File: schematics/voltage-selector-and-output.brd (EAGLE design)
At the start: 100 x 80 mm, 22 parts, among them IC1 3.3V, IC2 MIC2941, IC4 ULN2003AN, IC6 ATTINY85, IC7 74LS595N

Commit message: Finally updated the primary schematic
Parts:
- removed INPUT: (no value), SparkFun:1X02
- removed ISP1: AVRISP-6, adafruit:AVRISP
- removed JP1: (no value), SparkFun:JST-2-PTH
- removed R11: 10k, rcl-ez:0207/5V
- removed R7: 11k, rcl-ez:0207/5V
- removed R8: 20.5k, rcl-ez:0207/5V
- removed R9: 41.2k, rcl-ez:0207/5V
- removed R97: 6.49K 1%, rcl-ez:0207/5V
- added C1, C4: 47uF/25V, minimidi:E2,5-6
- added C5: 0.1uF, SparkFun-Capacitors:CAP-PTH-SMALL
- added D1, D2, D3, D4: 1N4007, gm-diodes:DO41-3
- added D6: (no value), SparkFun-LED:LED3MM-NS
- added IC3: MCP41010P, microchip-custom:DIL8
- added IC5: 12V, v-reg:78XXS
- added ISP: AVRISP-6, adafruit:AVRISP
- added JACK, XFRM: (no value), SparkFun:1X02
- added R2: 10k, rcl-ez:0207/5V
- added R3: 1K, rcl-ez:0207/5V
- added R4: 470, SparkFun-Resistors:AXIAL-0.4
- added TOGGLE: SPST, gm-switches:SPST
- moved IC4 94.2 mm to (-40.6, 6.35)
- moved POT 86.9 mm to (-20.3, 57.1)
- moved JP4 83.9 mm to (-48.3, 50.8)
- moved USB 74.2 mm to (-48.3, 57.1)
- moved IC7 54.8 mm to (-24.1, 25.4)
- moved IC6 54.6 mm to (-43.2, 24.1)
- moved R1 48.4 mm to (-59.7, 44.5)
- moved C3 41.5 mm to (-54.6, 35.6)
- moved IC1 30.7 mm to (-57.1, 27.9)
- moved IC2 26.2 mm to (-19.1, 40.6)
- moved METER 10.9 mm to (-27.9, 57.1)
- moved POSTS 10.9 mm to (-35.6, 57.1)
- moved C2 9.92 mm to (-38.1, 45.7)
- moved SOCKET 6.35 mm to (-57.1, 50.8)
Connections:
- net N$17 renamed PB4
- removed net ISP_VCC: IC1.OUT, IC6.8, ISP1.2, JP4.1
- removed net N$15: IC6.1, ISP1.5
- removed net N$16: IC6.2, IC7.11
- removed net N$18: IC6.7, IC7.12, ISP1.3
- removed net N$19: IC6.5, ISP1.4, JP4.2, R1.2
- removed net N$22: IC4.16, R7.2
- removed net N$23: IC6.6, IC7.14, ISP1.1
- removed net N$24: IC4.15, R8.2
- removed net N$25: IC4.14, R9.2
- removed net N$8: IC2.1, POT.2, R97.2
- new net IC_VCC: IC1.OUT, IC3.5, IC3.8, IC6.8, ISP.2, JP4.1
- new net N$2: D1.A, D3.C, XFRM.2
- new net N$3: D2.A, D4.C, XFRM.1
- new net N$4: IC2.1, IC3.6, R3.2
- new net N$5: D6.K, R4.P$2
- new net N$6: POT.2
- new net N$9: C4.+, D1.C, D2.C, TOGGLE.1
- new net PB0: IC6.5, ISP.4, JP4.2, R1.2
- new net PB1: IC3.3, IC6.6, IC7.14, ISP.5
- new net PB2: IC3.2, IC6.7, IC7.12, ISP.3
- new net PB3: IC3.1, IC6.2, IC7.11
- new net PB5: IC6.1, ISP.1
- new net RECTIFIED_12VCC: C1.+, C5.1, D6.A, IC1.IN, IC2.4, IC5.OUT
- net AGND: now also C1.-, C4.-, C5.2, D3.A, D4.A, IC3.4, IC3.7, IC5.GND, ISP.6, JACK.2, R2.2, R3.1, R4.P$1; no longer IC4.8, INPUT.1, ISP1.6, R11.2, R97.1
- net GND: now also IC4.8
- net N$1: now also IC5.IN, TOGGLE.2; no longer IC1.IN, IC2.4, INPUT.2
- net N$27: no longer IC4.1
- net N$28: no longer IC4.2
- net N$29: no longer IC4.3
- net N$30: no longer IC4.4
- net N$31: no longer IC4.5
- net N$34: now also R2.1; no longer R11.1
- net VADJ: now also JACK.1

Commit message: Changed the pin being used for the pot SI
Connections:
- net PB1: no longer IC3.3
- net PB5: now also IC3.3
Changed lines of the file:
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@@
 <contactref element="ISP" pad="1"/>
 <contactref element="IC6" pad="1"/>
+<contactref element="IC3" pad="3"/>
 <wire x1="-40.64" y1="38.1" x2="-46.99" y2="20.32" width="0" layer="19" extent="1-1"/>
+<wire x1="-20.32" y1="2.54" x2="-46.99" y2="20.32" width="0" layer="19" extent="1-1"/>
 </signal>
 <signal name="PB2">
@@
 <contactref element="ISP" pad="5"/>
 <contactref element="IC7" pad="14"/>
-<contactref element="IC3" pad="3"/>
-<wire x1="-27.94" y1="29.21" x2="-20.32" y2="2.54" width="0" layer="19" extent="1-1"/>
-<wire x1="-40.64" y1="33.02" x2="-27.94" y2="29.21" width="0" layer="19" extent="1-1"/>
-<wire x1="-41.91" y1="27.94" x2="-40.64" y2="33.02" width="0" layer="19" extent="1-1"/>
+<wire x1="-40.64" y1="33.02" x2="-41.91" y2="27.94" width="0" layer="19" extent="1-1"/>
+<wire x1="-27.94" y1="29.21" x2="-40.64" y2="33.02" width="0" layer="19" extent="1-1"/>
 </signal>
 <signal name="N$27">

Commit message: Resized board boundary to what I have room for and removed transistor array
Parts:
- removed IC4: ULN2003AN, uln-udn:DIL16
- added Q1: 2N3906, transistor-pnp:TO92
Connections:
- net GND: no longer IC4.8
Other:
- board size 100 x 80 mm -> 55.5 x 41.9 mm
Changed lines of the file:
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@@
 <board>
 <plain>
-<wire x1="0" y1="0" x2="100" y2="0" width="0" layer="20"/>
-<wire x1="100" y1="0" x2="100" y2="80" width="0" layer="20"/>
-<wire x1="100" y1="80" x2="0" y2="80" width="0" layer="20"/>
-<wire x1="0" y1="80" x2="0" y2="0" width="0" layer="20"/>
+<wire x1="0" y1="0" x2="55.55" y2="0" width="0" layer="20"/>
+<wire x1="55.55" y1="0" x2="55.55" y2="41.9" width="0" layer="20"/>
+<wire x1="55.55" y1="41.9" x2="0" y2="41.9" width="0" layer="20"/>
+<wire x1="0" y1="41.9" x2="0" y2="0" width="0" layer="20"/>
 </plain>
 <attributes>
@@
 <attribute name="MPN" value="MCP41010" x="-21.59" y="6.35" size="1.778" layer="27" display="off"/>
 </element>
-<element name="IC4" library="uln-udn" package="DIL16" value="ULN2003AN" x="-40.64" y="6.35"/>
 <element name="IC5" library="v-reg" package="78XXS" value="12V" x="-30.48" y="40.64"/>
 <element name="IC6" library="SparkFun" package="DIP08" value="ATTINY85" x="-43.18" y="24.13"/>
@@
 <element name="XFRM" library="SparkFun" package="1X02" value="" x="-41.91" y="57.15"/>
 <element name="JACK" library="SparkFun" package="1X02" value="" x="-60.96" y="-3.81"/>
+<element name="Q1" library="transistor-pnp" package="TO92" value="2N3906" x="-59.69" y="-8.89"/>
 </elements>
 <signals>
 <signal name="GND">
-<contactref element="IC4" pad="8"/>
 <contactref element="IC7" pad="8"/>
-<wire x1="-15.24" y1="21.59" x2="-31.75" y2="2.54" width="0" layer="19" extent="1-1"/>
 </signal>
 <signal name="VCC">

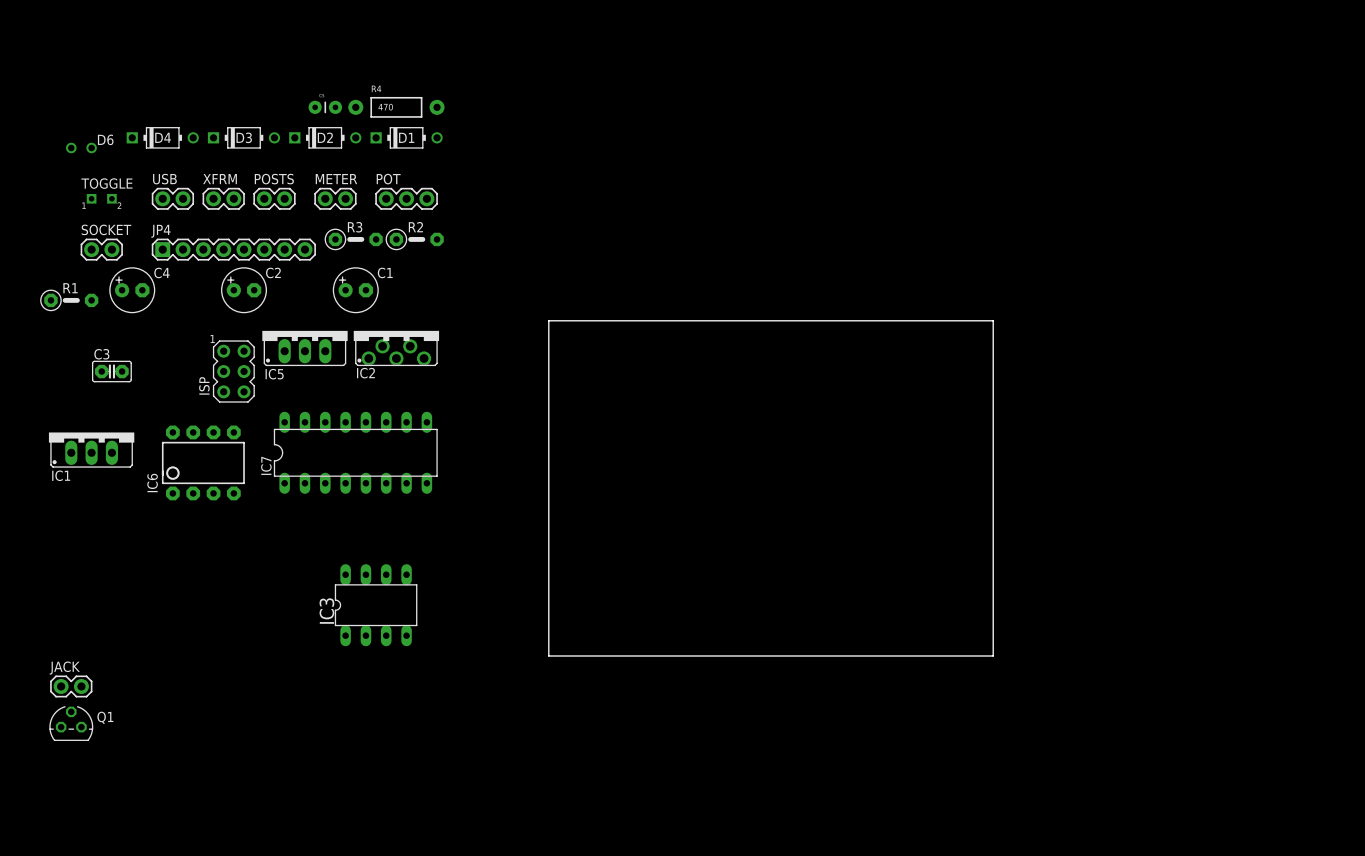
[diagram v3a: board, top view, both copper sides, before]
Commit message: Finally got to working on the main board layout
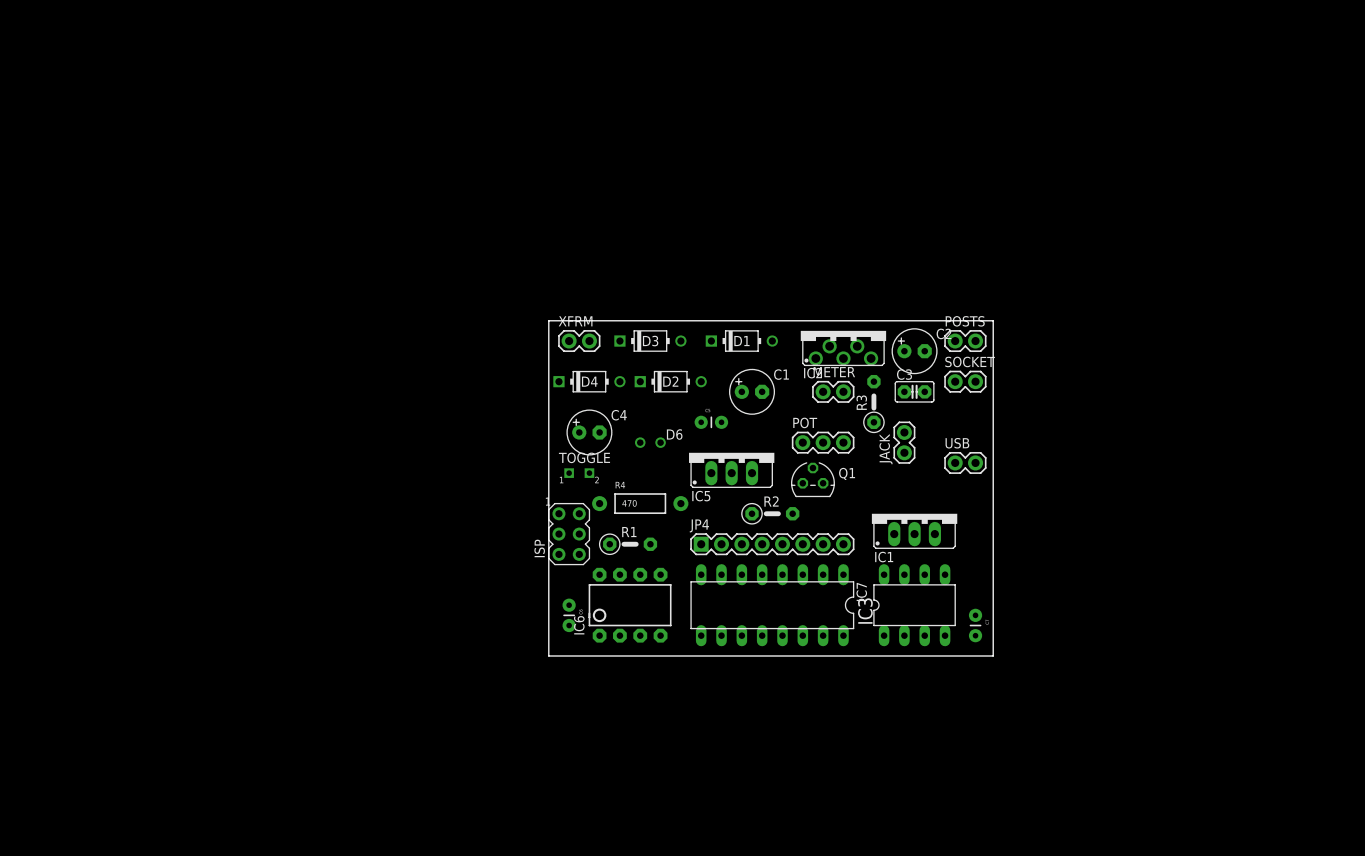
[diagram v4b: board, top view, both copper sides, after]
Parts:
- added C6, C7: 0.1uF, SparkFun-Capacitors:CAP-PTH-SMALL
- moved JACK 109.4 mm to (44.5, 25.4), turned to 90 degrees
- moved SOCKET 109.2 mm to (50.8, 34.3)
- moved USB 104.4 mm to (50.8, 24.1)
- moved IC1 103.4 mm to (45.7, 17.8)
- moved C3 100.4 mm to (45.7, 33.0)
- moved Q1 97.6 mm to (33.0, 21.6)
- moved POSTS 88.2 mm to (50.8, 39.4)
- moved C2 84.2 mm to (45.7, 38.1)
- moved D6 80.1 mm to (12.7, 26.7)
- moved JP4 76.7 mm to (19.1, 14.0)
- moved R1 76.2 mm to (10.2, 14.0)
- moved TOGGLE 68.8 mm to (3.81, 22.9)
- moved R3 67.9 mm to (40.6, 31.8), turned to 90 degrees
- moved IC3 67.3 mm to (45.7, 6.35)
- moved METER 66.7 mm to (34.3, 33.0)
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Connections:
- new net N$7: POT.3, Q1.1
- net AGND: now also C6.2, C7.2, Q1.3; no longer POT.3
- net IC_VCC: now also C6.1, C7.1

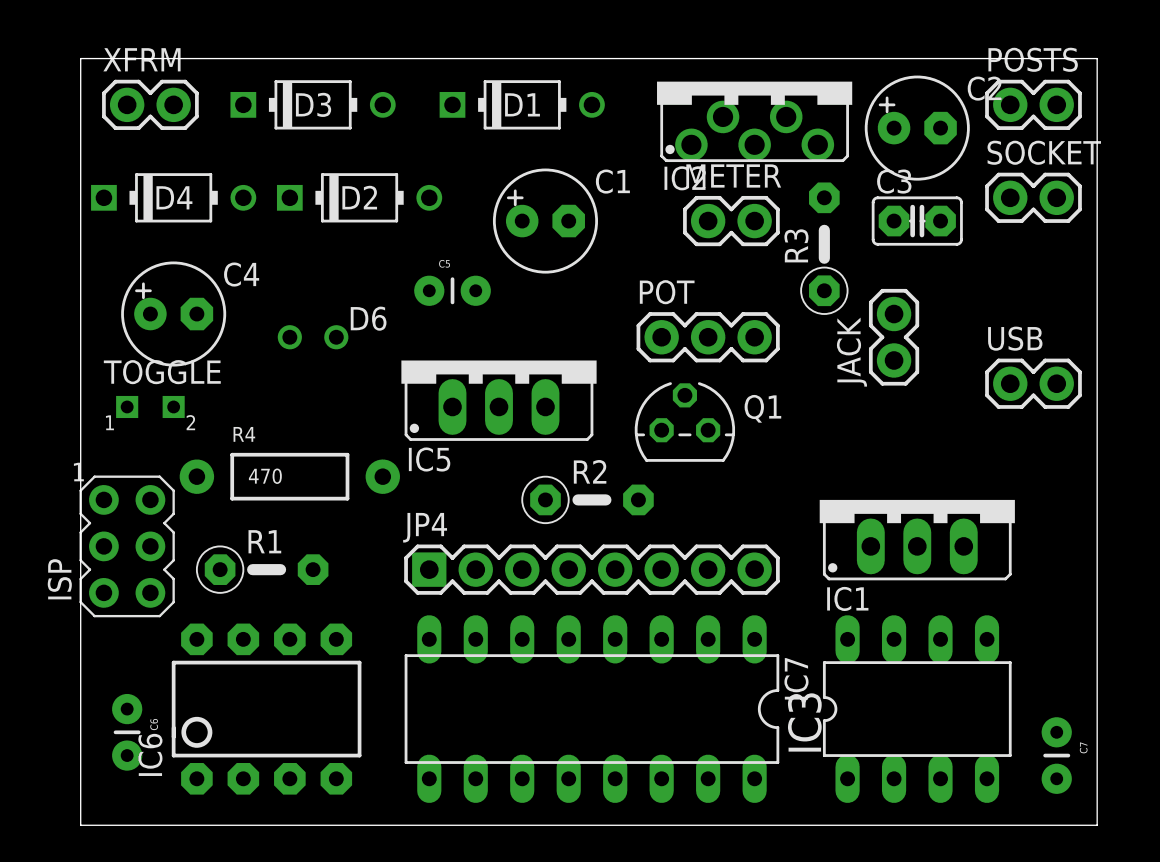
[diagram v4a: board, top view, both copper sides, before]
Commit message: Moved the shift register to the top board since I have more room there and on the bottom board and I get to free up some pins on the jumper
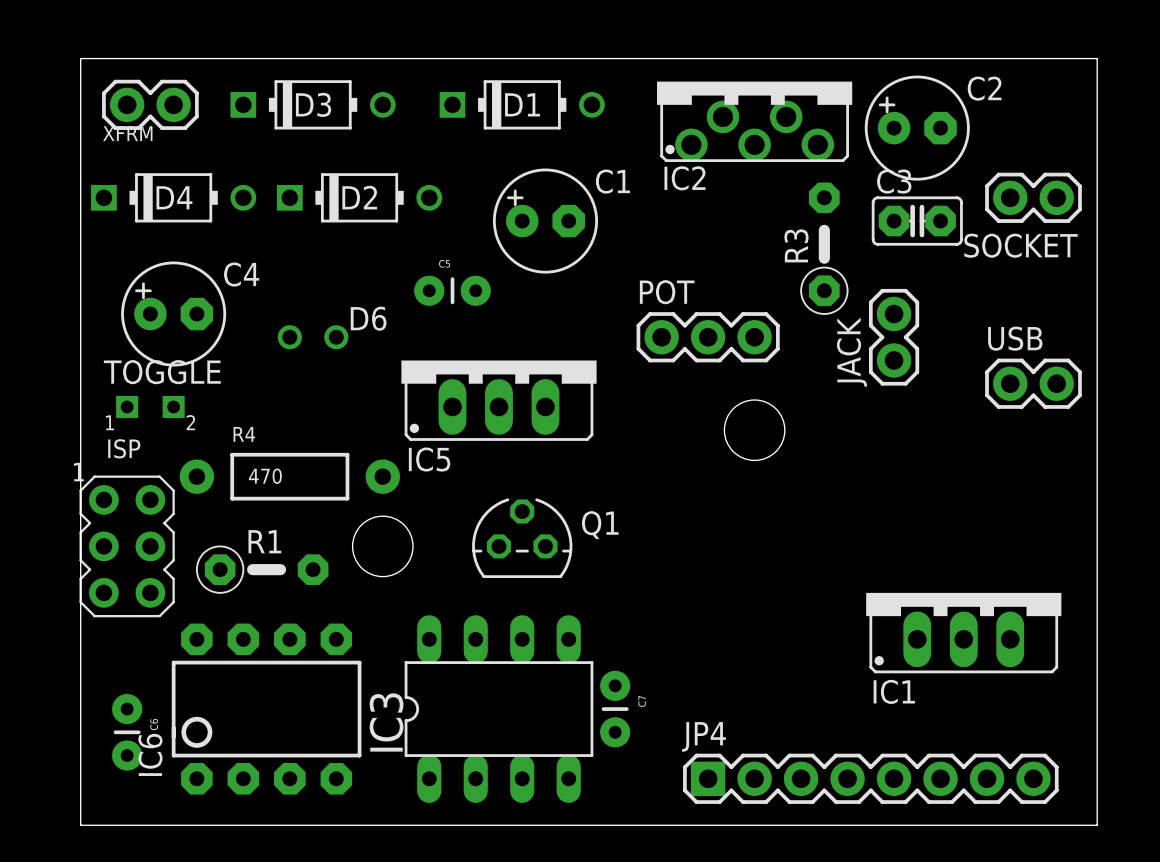
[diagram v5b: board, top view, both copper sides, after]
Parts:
- removed IC7: 74LS595N, 74xx-us:DIL16
- removed METER, POSTS: (no value), SparkFun:1X02
- removed R2: 10k, rcl-ez:0207/5V
- added STANDOFF1, STANDOFF2: STAND-OFF, SparkFun-Electromechanical:STAND-OFF
- moved C7 24.3 mm to (29.2, 7.62)
- moved IC3 22.9 mm to (22.9, 6.35)
- moved JP4 19.0 mm to (34.3, 2.54)
- moved Q1 10.9 mm to (24.1, 15.2)
- moved IC1 5.68 mm to (48.3, 12.7)
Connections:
- removed net GND: IC7.8
- removed net N$27: IC7.1, JP4.7
- removed net N$28: IC7.2, JP4.6
- removed net N$29: IC7.3, JP4.5
- removed net N$30: IC7.4, JP4.4
- removed net N$31: IC7.5, JP4.3
- removed net N$34: IC7.13, IC7.9, R2.1
- removed net VCC: IC7.16
- net AGND: no longer METER.2, POSTS.2, R2.2
- net PB0: now also JP4.3; no longer JP4.2
- net PB1: now also JP4.4; no longer IC7.14
- net PB2: now also JP4.5; no longer IC7.12
- net PB3: now also JP4.6; no longer IC7.11
- net PB4: now also JP4.7; no longer IC7.10
- net VADJ: now also JP4.2; no longer METER.1, POSTS.1

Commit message: Doing this instead of working out. Yup
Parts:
- IC1: value 3.3V -> 5V
- moved IC1 8.89 mm to (39.4, 12.7)
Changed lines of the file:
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@@
 </element>
 <element name="D6" library="SparkFun-LED" package="LED3MM-NS" value="" x="12.7" y="26.67"/>
-<element name="IC1" library="v-reg" package="78XXS" value="3.3V" x="48.26" y="12.7"/>
+<element name="IC1" library="v-reg" package="78XXS" value="5V" x="39.37" y="12.7"/>
 <element name="IC2" library="bbsup" package="TO220-5" value="MIC2941" x="36.83" y="40.64"/>
 <element name="IC3" library="microchip-custom" package="DIL8" value="MCP41010P" x="22.86" y="6.35">
@@
 <contactref element="C7" pad="1"/>
 <contactref element="C6" pad="1"/>
-<wire x1="34.29" y1="2.54" x2="50.8" y2="10.16" width="0" layer="19" extent="1-1"/>
+<wire x1="34.29" y1="2.54" x2="41.91" y2="10.16" width="0" layer="19" extent="1-1"/>
 <wire x1="29.21" y1="7.62" x2="34.29" y2="2.54" width="0" layer="19" extent="1-1"/>
 <wire x1="26.67" y1="10.16" x2="29.21" y2="7.62" width="0" layer="19" extent="1-1"/>
@@
 <wire x1="3.81" y1="12.7" x2="7.62" y2="13.97" width="0" layer="19" extent="1-1"/>
 <wire x1="2.54" y1="3.81" x2="3.81" y2="12.7" width="0" layer="19" extent="1-1"/>
-<wire x1="48.26" y1="10.16" x2="53.34" y2="24.13" width="0" layer="19" extent="1-1"/>
-<wire x1="52.07" y1="2.54" x2="48.26" y2="10.16" width="0" layer="19" extent="1-1"/>
+<wire x1="39.37" y1="10.16" x2="53.34" y2="24.13" width="0" layer="19" extent="1-1"/>
+<wire x1="52.07" y1="2.54" x2="39.37" y2="10.16" width="0" layer="19" extent="1-1"/>
 </signal>
 <signal name="PB5">
@@
 <wire x1="11.43" y1="26.67" x2="19.05" y2="29.21" width="0" layer="19" extent="1-1"/>
 <wire x1="25.4" y1="22.86" x2="19.05" y2="29.21" width="0" layer="19" extent="1-1"/>
-<wire x1="45.72" y1="10.16" x2="25.4" y2="22.86" width="0" layer="19" extent="1-1"/>
+<wire x1="36.83" y1="10.16" x2="25.4" y2="22.86" width="0" layer="19" extent="1-1"/>
 </signal>
 <signal name="N$2">
